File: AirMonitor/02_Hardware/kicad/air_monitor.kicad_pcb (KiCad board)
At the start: 4 copper layers, 64 x 64 mm, 5 parts, among them J1 FH12-31S-0.5SH, J2 FH12-6S-0.5SH, U1 ESP32-WROVER-B, U2 TPS62088

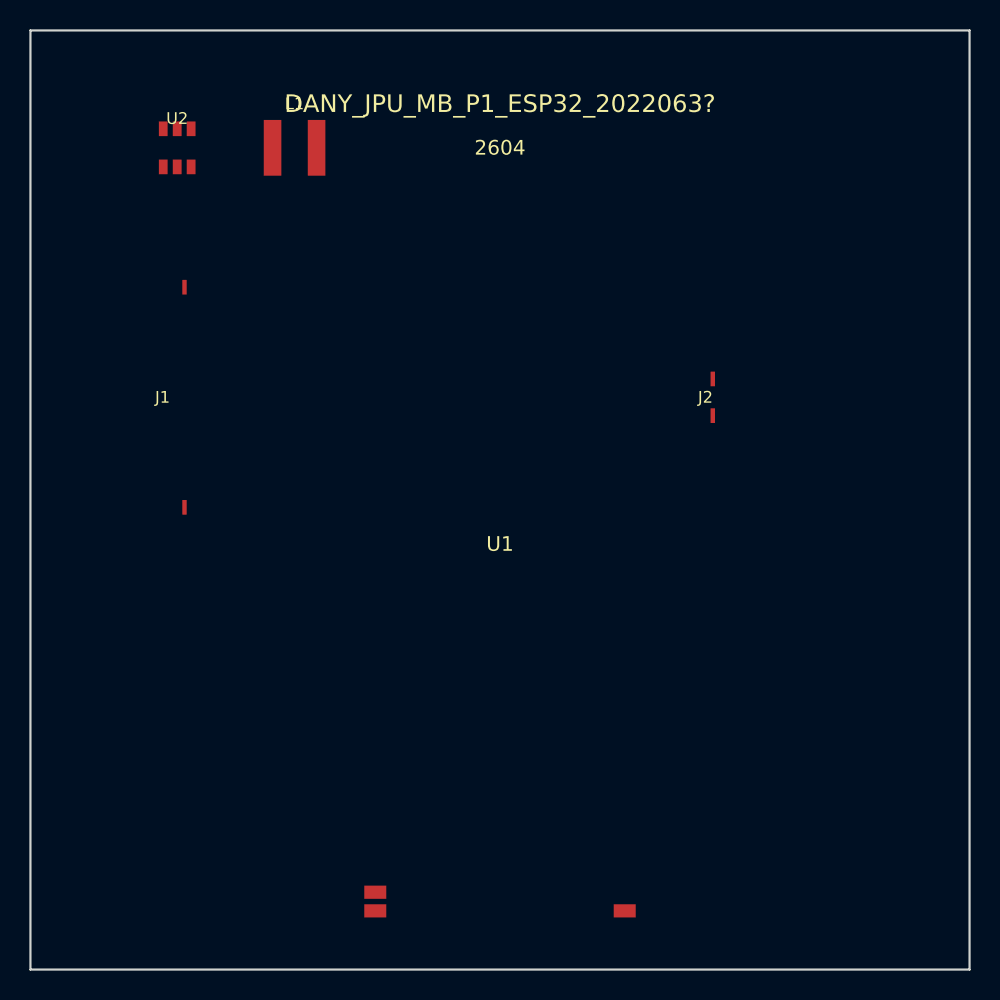
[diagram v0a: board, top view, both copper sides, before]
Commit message: Update MCU identification to STM32F407ZGT6 and generate STIST PBL project report
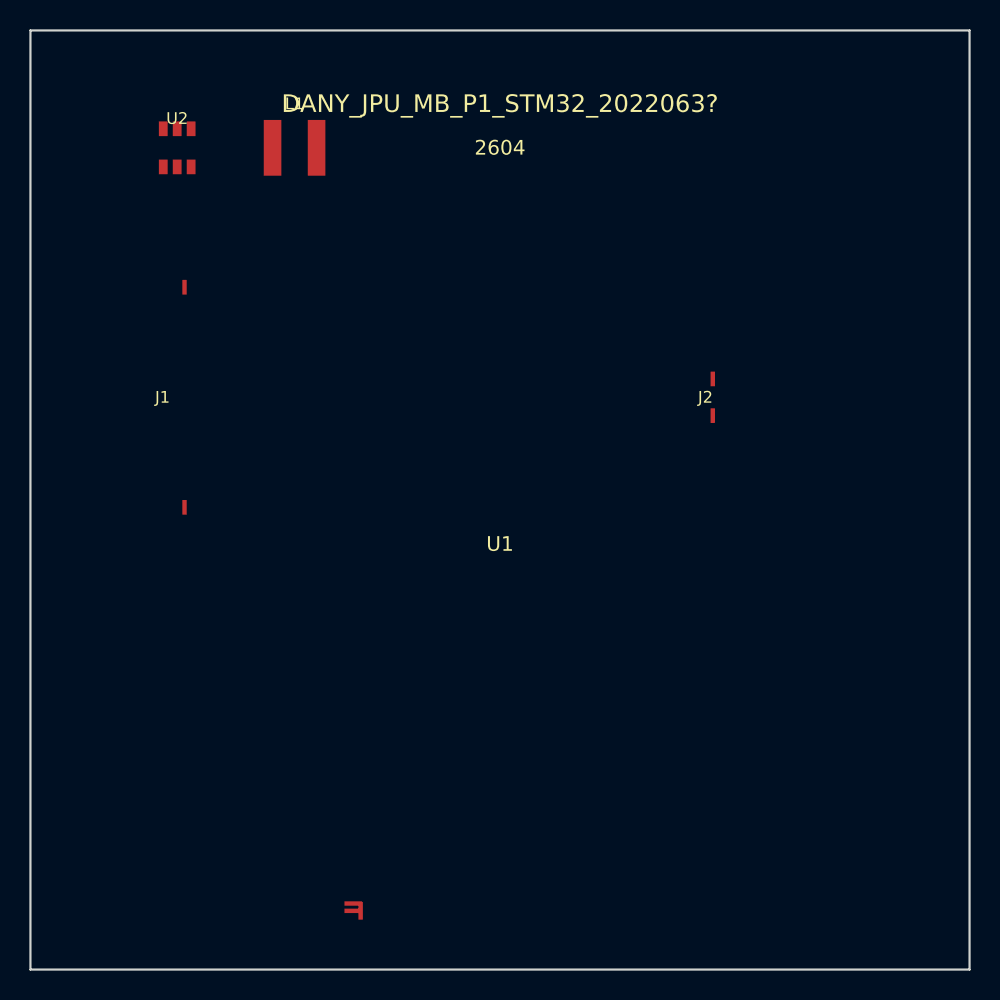
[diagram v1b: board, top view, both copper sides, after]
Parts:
- U1: value ESP32-WROVER-B -> STM32F407ZGT6; footprint RF_Module:ESP32-WROVER-B -> Package_QFP:LQFP-144_20x20mm_P0.5mm
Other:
- board text added: "DANY_JPU_MB_P1_STM32_2022063?"
- board text removed: "DANY_JPU_MB_P1_ESP32_2022063?"
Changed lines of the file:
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@@
 		(rev "Rev 1.0")
 		(company "Air Monitor Engineering Team")
-		(comment 1 "Core MCU: Espressif ESP32-WROVER-B")
+		(comment 1 "Core MCU: STMicroelectronics STM32F407ZGT6 (LQFP-144)")
 		(comment 2 "Layer Stackup: 4-Layer FR4 1.6mm")
 		(comment 3 "Dimensions: 64.0mm x 64.0mm")
@@
 		(layer "Edge.Cuts")
 	)
-	(gr_text "DANY_JPU_MB_P1_ESP32_2022063?"
+	(gr_text "DANY_JPU_MB_P1_STM32_2022063?"
 		(at 132 105)
 		(layer "F.SilkS")
@@
 		(effects (font (size 1.0 1.0) (thickness 0.18)))
 	)
-	(footprint "RF_Module:ESP32-WROVER-B"
+	(footprint "Package_QFP:LQFP-144_20x20mm_P0.5mm"
 		(layer "F.Cu")
 		(at 132 150)
-		(descr "Espressif ESP32-WROVER-B module, antenna overhang at bottom edge")
+		(descr "STMicroelectronics STM32F407ZGT6 ARM Cortex-M4 MCU, LQFP-144 20x20mm")
 		(property "Reference" "U1" (at 0 -15) (layer "F.SilkS") (effects (font (size 1 1) (thickness 0.15))))
-		(property "Value" "ESP32-WROVER-B" (at 0 -13) (layer "F.Fab") (effects (font (size 1 1) (thickness 0.15))))
-		(pad "1" smd rect (at -8.5 10) (size 1.5 0.9) (layers "F.Cu" "F.Paste" "F.Mask") (net 1 "GND"))
-		(pad "2" smd rect (at -8.5 8.73) (size 1.5 0.9) (layers "F.Cu" "F.Paste" "F.Mask") (net 2 "3V3_SYS"))
-		(pad "38" smd rect (at 8.5 10) (size 1.5 0.9) (layers "F.Cu" "F.Paste" "F.Mask") (net 1 "GND"))
+		(property "Value" "STM32F407ZGT6" (at 0 -13) (layer "F.Fab") (effects (font (size 1 1) (thickness 0.15))))
+		(pad "1" smd rect (at -10 10) (size 1.2 0.3) (layers "F.Cu" "F.Paste" "F.Mask") (net 1 "GND"))
+		(pad "2" smd rect (at -10 9.5) (size 1.2 0.3) (layers "F.Cu" "F.Paste" "F.Mask") (net 2 "3V3_SYS"))
+		(pad "144" smd rect (at -9.5 10) (size 0.3 1.2) (layers "F.Cu" "F.Paste" "F.Mask") (net 1 "GND"))
 	)
 	(footprint "Connector_FFC-FPC:Hirose_FH12-31S-0.5SH_1x31-1MP_P0.50mm_Horizontal"
